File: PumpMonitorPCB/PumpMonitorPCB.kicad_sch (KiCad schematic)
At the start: 17 parts, among them J1 Mains terminals, K1 J115F11CH5VDCS61-5U Relay, Q1 AS2302, U1 AMS1117-3.3, U2 ACS770xCB-050B-PFF, U3 ESP32-C6-WROOM-1U-N8

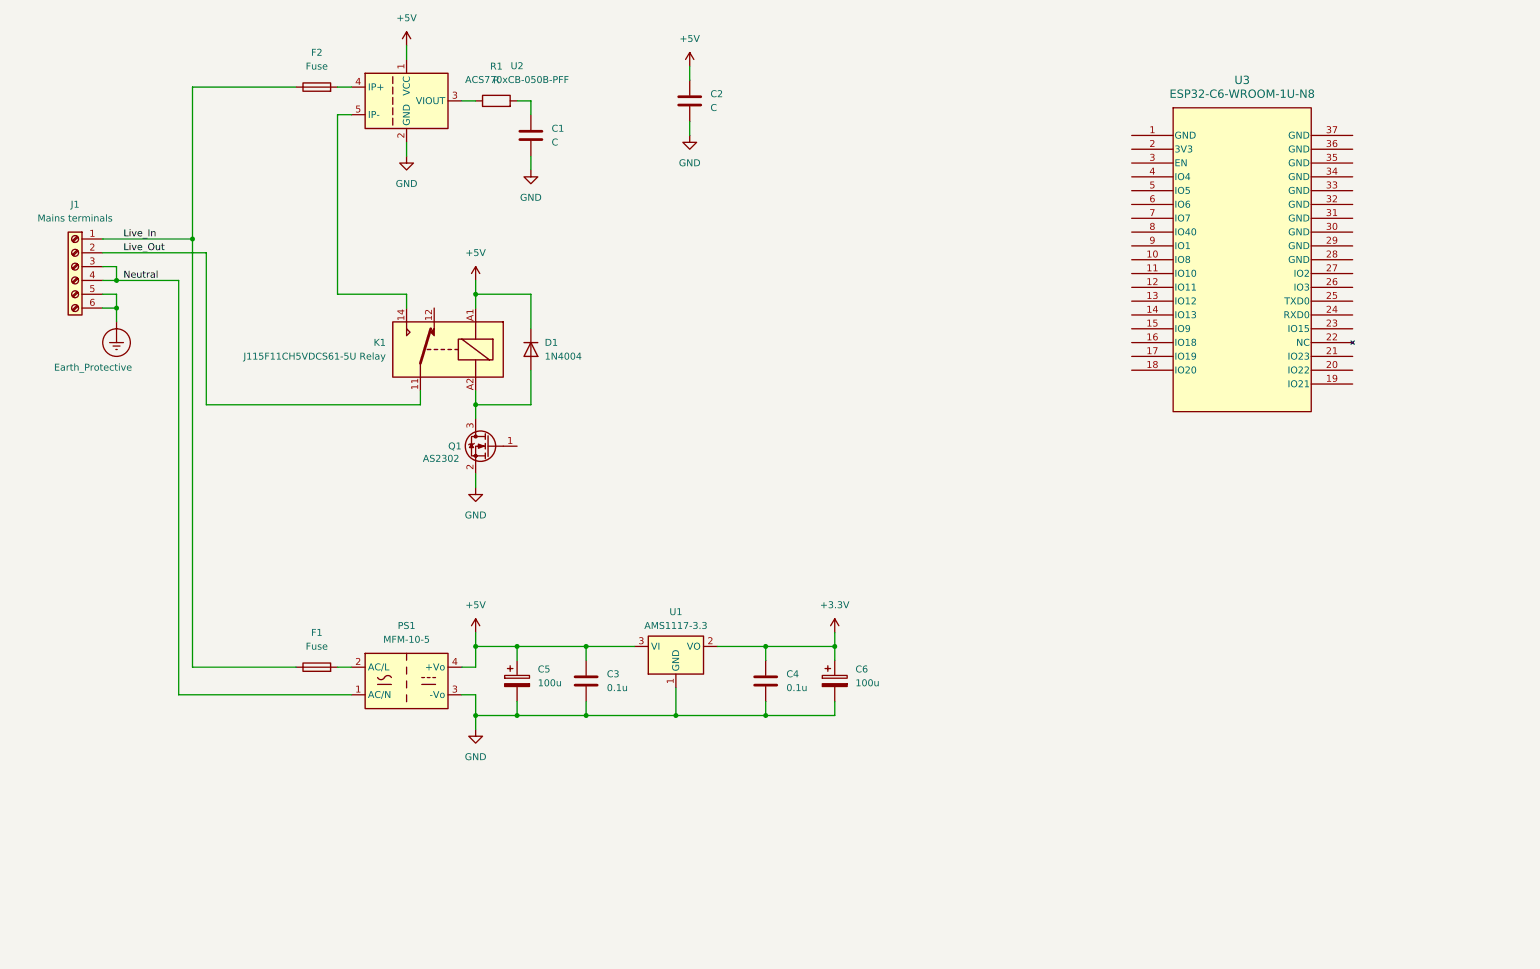
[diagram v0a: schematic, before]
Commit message: Rearranging to include a wiring diagram and contactor.
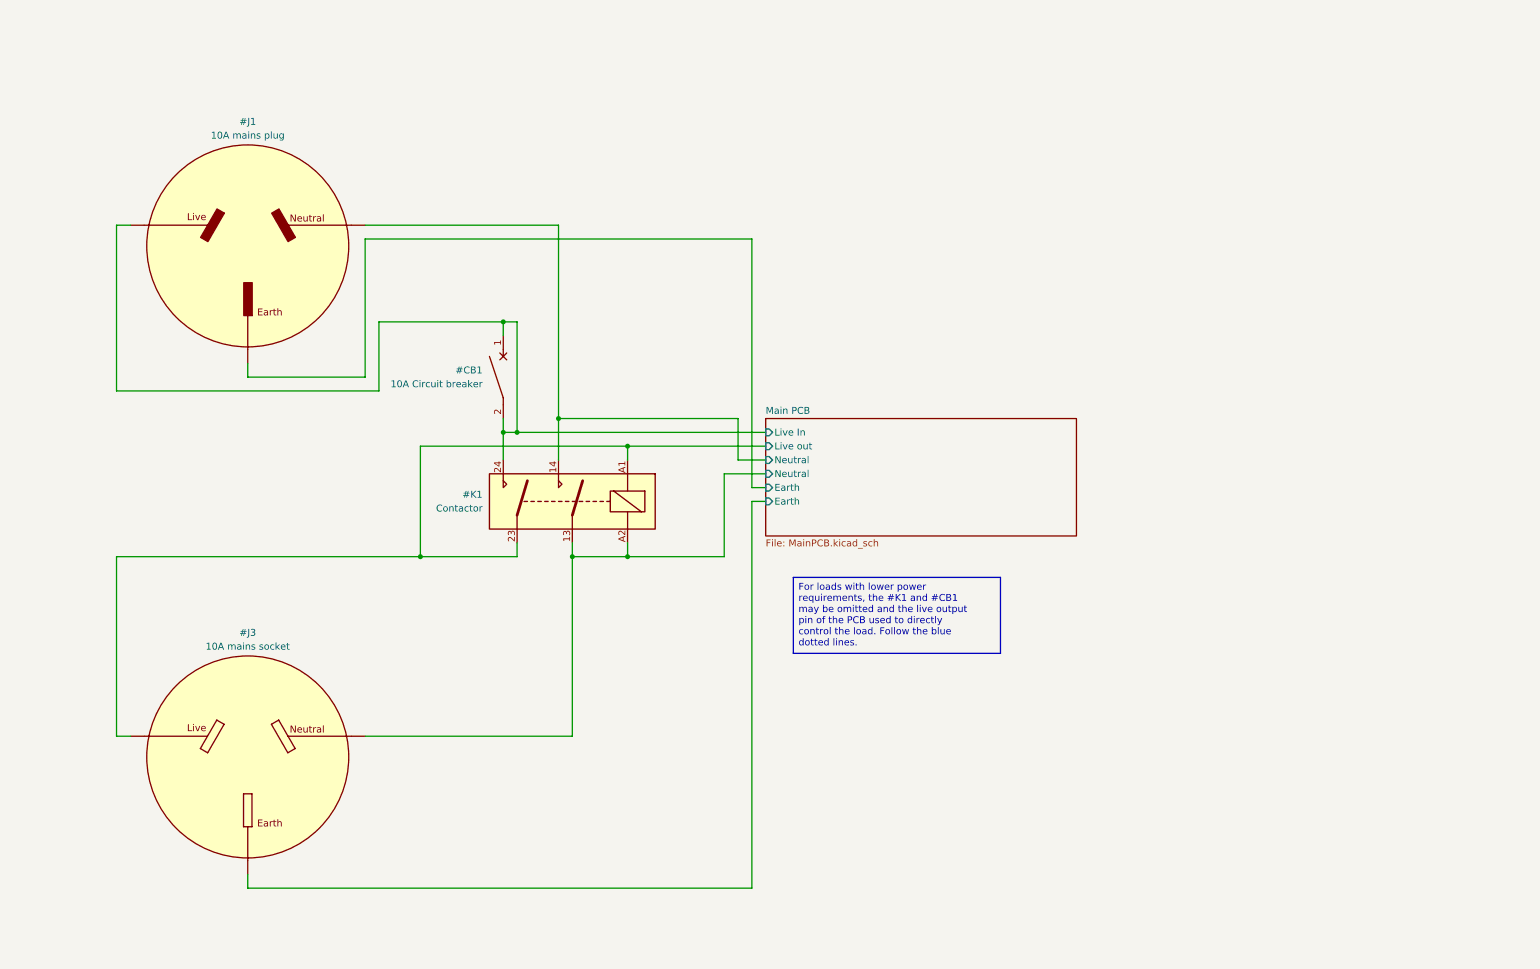
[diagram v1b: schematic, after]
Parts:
- removed C1, C2: C, symbol Device:C
- removed C3, C4: 0.1u, symbol Device:C
- removed C5, C6: 100u, symbol Device:C_Polarized
- removed D1: 1N4004, Diode_THT:D_DO-41_SOD81_P10.16mm_Horizontal, symbol Diode:1N4004
- removed F1, F2: Fuse, symbol Device:Fuse
- removed J1: Mains terminals, symbol Connector:Screw_Terminal_01x06
- removed K1: J115F11CH5VDCS61-5U Relay, J115F11CH5VDCS61_5U_Relay:J115F11CH5VDCS61-5U, symbol Relay:Relay_SPDT
- removed PS1: MFM-10-5, Converter_ACDC:Converter_ACDC_MeanWell_MFM-10-xx_THT, symbol Converter_ACDC:MFM-10-5
- removed Q1: AS2302, Package_TO_SOT_SMD:TSOT-23, symbol Device:Q_NMOS_GSD
- removed R1: R, symbol Device:R
- removed U1: AMS1117-3.3, Package_TO_SOT_SMD:SOT-223-3_TabPin2, symbol Regulator_Linear:AMS1117-3.3
- removed U2: ACS770xCB-050B-PFF, Sensor_Current:Allegro_CB_PFF, symbol Sensor_Current:ACS770xCB-050B-PFF
- removed U3: ESP32-C6-WROOM-1U-N8, ESP32_C6_WROOM_1U_N8:MOD28_ESP32-C6-WROOM-1U_EXP, symbol ESP32_C6_WROOM_1U_N8:ESP32-C6-WROOM-1U-N8
- added #CB1: 10A Circuit breaker, symbol Device:CircuitBreaker_1P
- added #J1: 10A mains plug, symbol AustralianPowerpoints:3PinMainsPowerPlug
- added #J3: 10A mains socket, symbol AustralianPowerpoints:3PinMainsPowerSocket
- added #K1: Contactor, symbol Relay:Relay_DPST-NO
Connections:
- new net Main PCB/Earth: #J3.3 (Earth)
- new net Main PCB/Earth: #J1.3 (Earth)
- new net Main PCB/Live In: #CB1.1, #CB1.2, #J1.1 (Live), #K1.24
- new net Main PCB/Live out: #J3.1 (Live), #K1.23, #K1.A1
- new net Main PCB/Neutral: #J3.2 (Neutral), #K1.13, #K1.A2
- new net Main PCB/Neutral: #J1.2 (Neutral), #K1.14
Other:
- added sheet Main PCB (MainPCB.kicad_sch)
- title: Pump monitor -> Pump monitor - Wiring diagram

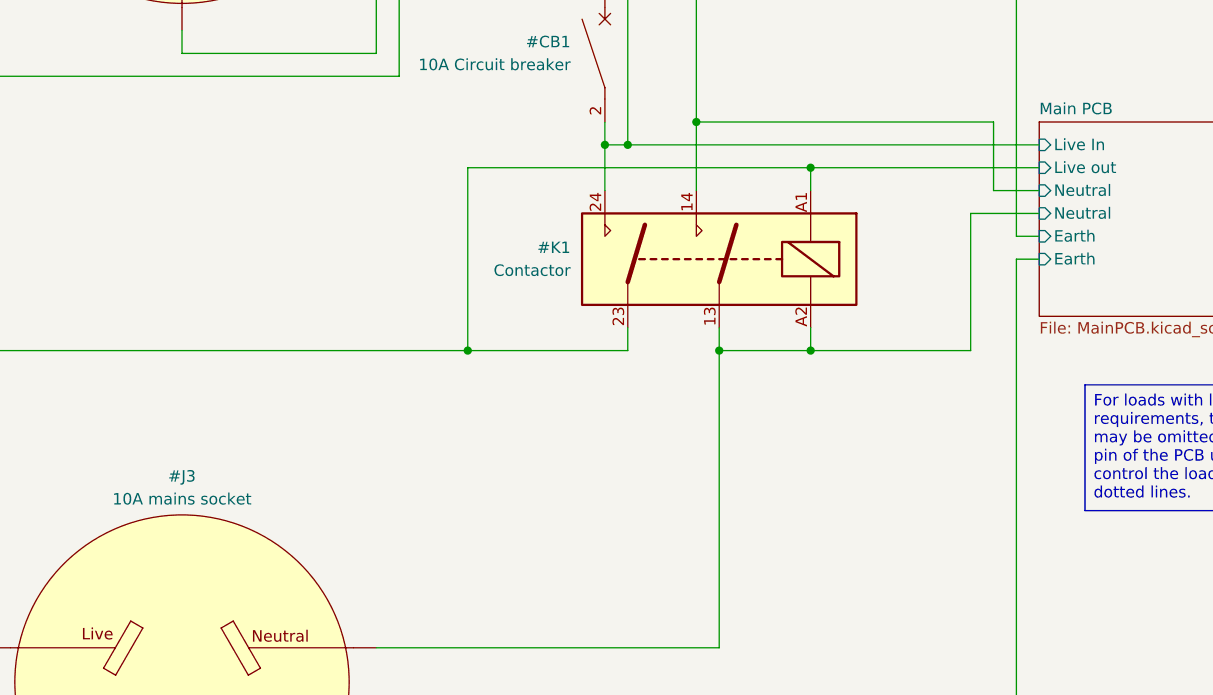
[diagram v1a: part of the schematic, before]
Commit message: Adding microcontroller, USB, UI components.
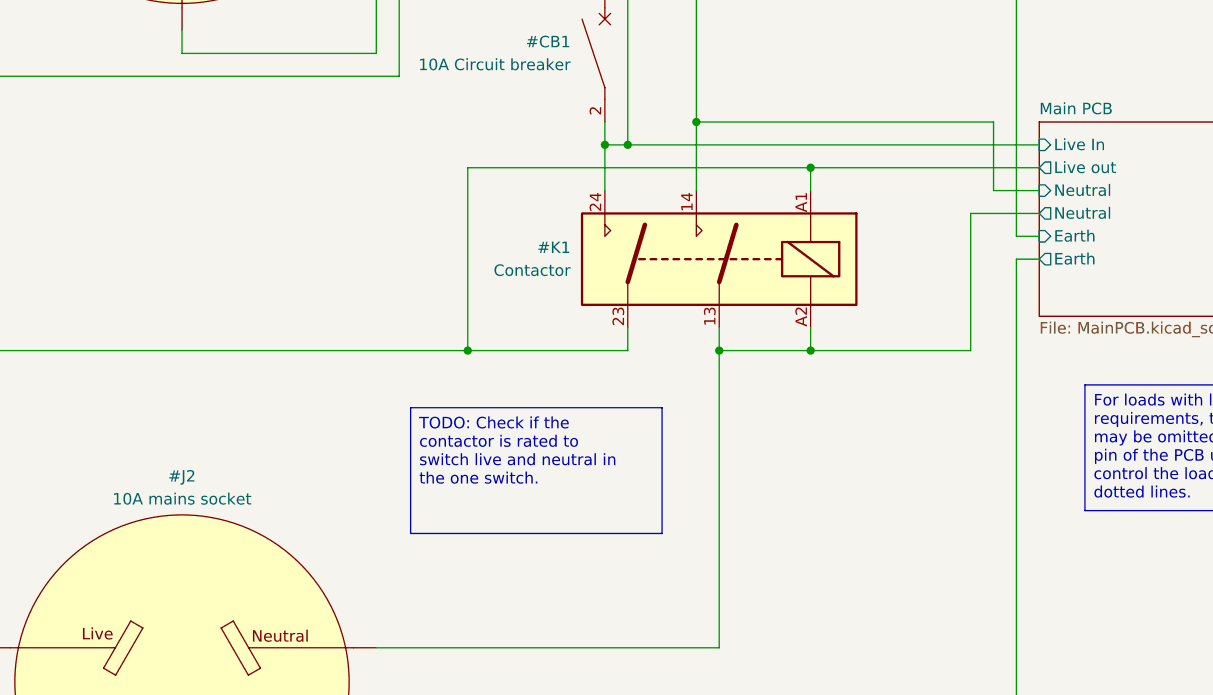
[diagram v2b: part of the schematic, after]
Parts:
- renumbered #J3 to #J2
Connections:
- net Main PCB/Earth is gone; now on net Main PCB/Earth: #J1.3 (Earth)
- net Main PCB/Neutral is gone; now on net Main PCB/Neutral: #J1.2 (Neutral), #K1.14
- net Main PCB/Earth: no longer #J2.3 (Earth)
- net Main PCB/Neutral: no longer #J2.2 (Neutral), #K1.13, #K1.A2
- new net Main PCB/Earth: #J2.3 (Earth)
- new net Main PCB/Neutral: #J2.2 (Neutral), #K1.13, #K1.A2
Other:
- title: Pump monitor - Wiring diagram -> Pump monitor - wiring diagram
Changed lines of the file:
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@@
 	(paper "A4")
 	(title_block
-		(title "Pump monitor - Wiring diagram")
-		(date "2025-09-11")
+		(title "Pump monitor - wiring diagram")
+		(date "2025-09-16")
 		(rev "V0.0.0")
 		(company "Jotham Gates")
@@
 		(at 163.83 123.19 0)
 		(size 38.1 13.97)
+		(margins 0.9525 0.9525 0.9525 0.9525)
+		(stroke
+			(width 0)
+			(type solid)
+		)
+		(fill
+			(type none)
+		)
+		(effects
+			(font
+				(size 1.27 1.27)
+			)
+			(justify left top)
+		)
+	)
+	(text_box "TODO: Check if the contactor is rated to switch live and neutral in the one switch."
+		(exclude_from_sim no)
+		(at 88.9 125.73 0)
+		(size 27.94 13.97)
 		(margins 0.9525 0.9525 0.9525 0.9525)
 		(stroke
@@
 		(dnp no)
 		(fields_autoplaced yes)
-		(property "Reference" "#J3"
+		(property "Reference" "#J2"
 			(at 63.5 133.35 0)
 			(effects
@@
 			(project ""
 				(path "/c90c4964-ca1b-44d9-8ea9-8989903af0f2"
-					(reference "#J3")
+					(reference "#J2")
 					(unit 1)
 				)
@@
 			)
 		)
-		(pin "Earth" input
+		(pin "Earth" output
 			(at 158.75 109.22 180)
 			(effects
@@
 			)
 		)
-		(pin "Live out" input
+		(pin "Live out" output
 			(at 158.75 99.06 180)
 			(effects
@@
 			)
 		)
-		(pin "Neutral" input
+		(pin "Neutral" output
 			(at 158.75 104.14 180)
 			(effects

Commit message: Tidied schematic, added LoRa module.
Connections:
- net Main PCB/Earth is gone; now on net Main PCB/Earth: #J1.3 (Earth)
- net Main PCB/Neutral is gone; now on net Main PCB/Neutral: #J1.2 (Neutral), #K1.14
- net Main PCB/Earth: no longer #J2.3 (Earth)
- net Main PCB/Neutral: no longer #J2.2 (Neutral), #K1.13, #K1.A2
- new net Main PCB/Earth: #J2.3 (Earth)
- new net Main PCB/Neutral: #J2.2 (Neutral), #K1.13, #K1.A2
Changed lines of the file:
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@@
 	(title_block
 		(title "Pump monitor - wiring diagram")
-		(date "2025-09-16")
+		(date "2025-09-25")
 		(rev "V0.0.0")
 		(company "Jotham Gates")

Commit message: Added op amps to voltage and current measurement, more footprint assignments.
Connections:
- net Main PCB/Earth is gone; now on net Main PCB/Earth: #J1.3 (Earth)
- net Main PCB/Neutral is gone; now on net Main PCB/Neutral: #J1.2 (Neutral), #K1.14
- net Main PCB/Earth: no longer #J2.3 (Earth)
- net Main PCB/Neutral: no longer #J2.2 (Neutral), #K1.13, #K1.A2
- new net Main PCB/Earth: #J2.3 (Earth)
- new net Main PCB/Neutral: #J2.2 (Neutral), #K1.13, #K1.A2
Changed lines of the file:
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@@
 		(rev "V0.0.0")
 		(company "Jotham Gates")
+		(comment 4 "Warning: Parts of this circuit operate at mains potential.")
 	)
 	(text_box "For loads with lower power requirements, the #K1 and #CB1 may be omitted and the live output pin of the PCB used to directly control the load. Follow the blue dotted lines."

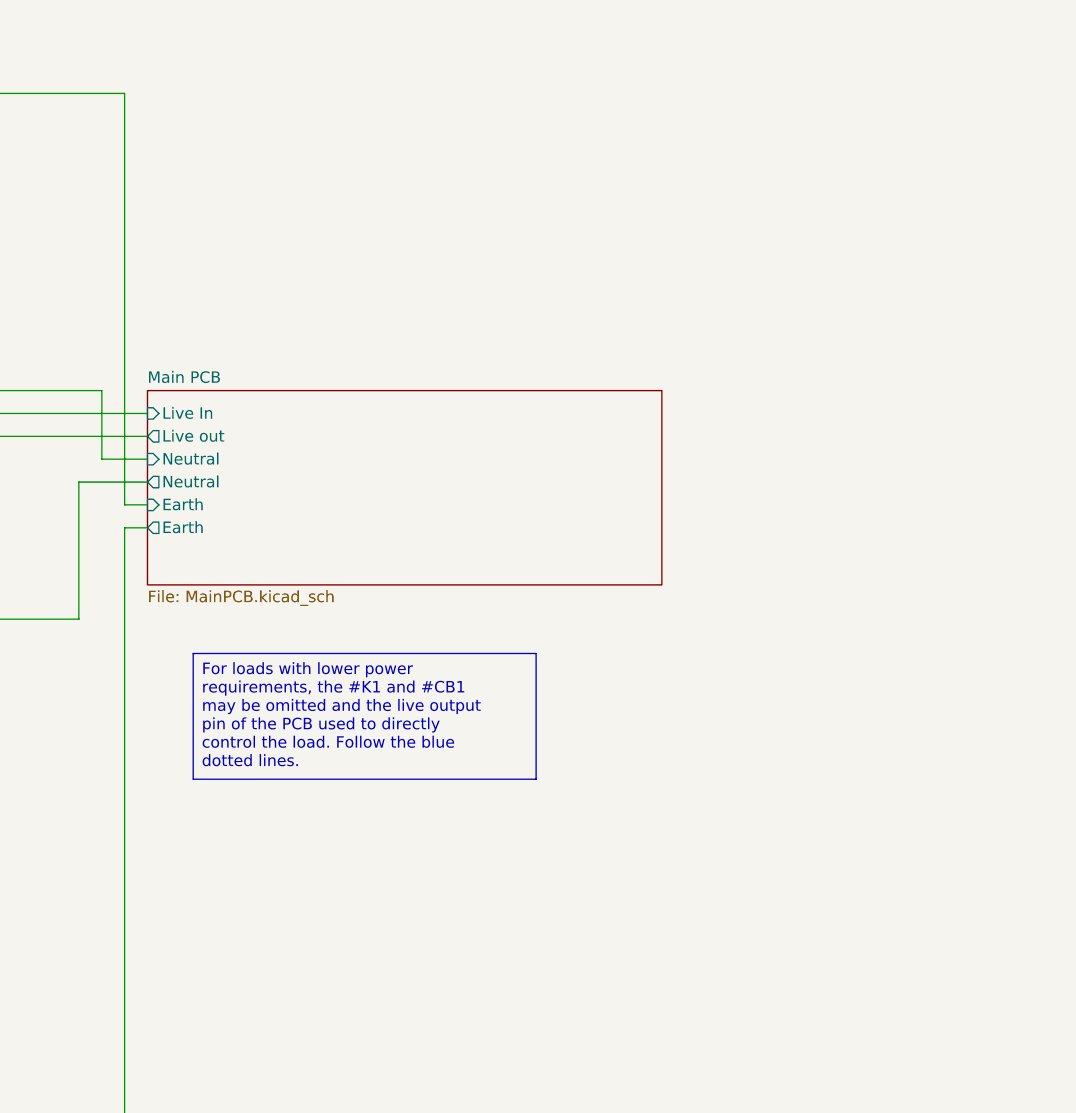
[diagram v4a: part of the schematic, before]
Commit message: Swapped current measurement to neutral (wiring diagram needs updating).
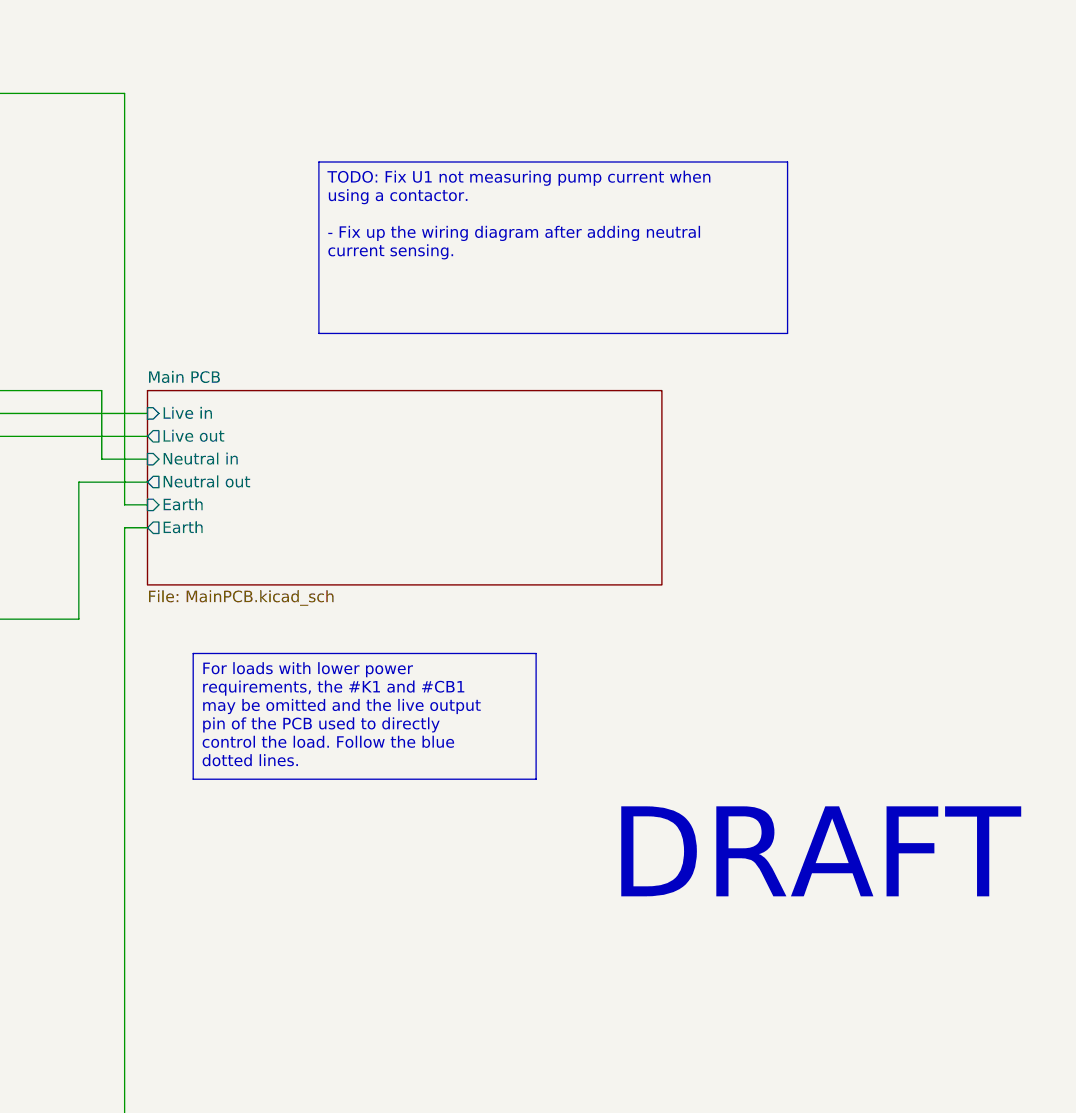
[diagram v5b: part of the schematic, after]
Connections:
- net Main PCB/Earth is gone; now on net Main PCB/Earth: #J1.3 (Earth)
- net Main PCB/Earth: no longer #J2.3 (Earth)
- net Main PCB/Live In renamed Main PCB/Live in
- net Main PCB/Neutral renamed Main PCB/Neutral out
- net Main PCB/Neutral renamed Main PCB/Neutral in
- new net Main PCB/Earth: #J2.3 (Earth)
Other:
- sheet Main PCB ports: added Live in, Neutral in, Neutral out; removed Live In, Neutral
- note added: "DRAFT"
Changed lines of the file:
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@@
 		(comment 4 "Warning: Parts of this circuit operate at mains potential.")
+	)
+	(text "DRAFT"
+		(exclude_from_sim no)
+		(at 232.918 145.796 0)
+		(effects
+			(font
+				(size 10 10)
+			)
+		)
 	)
 	(text_box "For loads with lower power requirements, the #K1 and #CB1 may be omitted and the live output pin of the PCB used to directly control the load. Follow the blue dotted lines."
@@
 		(at 163.83 123.19 0)
 		(size 38.1 13.97)
+		(margins 0.9525 0.9525 0.9525 0.9525)
+		(stroke
+			(width 0)
+			(type solid)
+		)
+		(fill
+			(type none)
+		)
+		(effects
+			(font
+				(size 1.27 1.27)
+			)
+			(justify left top)
+		)
+	)
+	(text_box "TODO: Fix U1 not measuring pump current when using a contactor.\n\n- Fix up the wiring diagram after adding neutral current sensing."
+		(exclude_from_sim no)
+		(at 177.8 68.58 0)
+		(size 52.07 19.05)
 		(margins 0.9525 0.9525 0.9525 0.9525)
 		(stroke
@@
 			)
 		)
-		(pin "Live In" input
-			(at 158.75 96.52 180)
-			(effects
-				(font
-					(size 1.27 1.27)
-				)
-				(justify left)
-			)
-		)
 		(pin "Live out" output
 			(at 158.75 99.06 180)
@@
 			)
 		)
-		(pin "Neutral" input
-			(at 158.75 101.6 180)
-			(effects
-				(font
-					(size 1.27 1.27)
-				)
-				(justify left)
-			)
-		)
 		(pin "Earth" input
 			(at 158.75 106.68 180)
@@
 			)
 		)
-		(pin "Neutral" output
+		(pin "Live in" input
+			(at 158.75 96.52 180)
+			(effects
+				(font
+					(size 1.27 1.27)
+				)
+				(justify left)
+			)
+		)
+		(pin "Neutral in" input
+			(at 158.75 101.6 180)
+			(effects
+				(font
+					(size 1.27 1.27)
+				)
+				(justify left)
+			)
+		)
+		(pin "Neutral out" output
 			(at 158.75 104.14 180)
 			(effects
